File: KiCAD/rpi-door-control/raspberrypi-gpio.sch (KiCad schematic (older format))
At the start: 26 parts, among them IC1 4N35, J1 RJ45, P1 CONN_13X2, P2 CONN_2, P3 CONN_2, P4 CONN_2, Q1 2N3904, Q2 2N3904, SW1 SW_PUSH, U1 RELAY

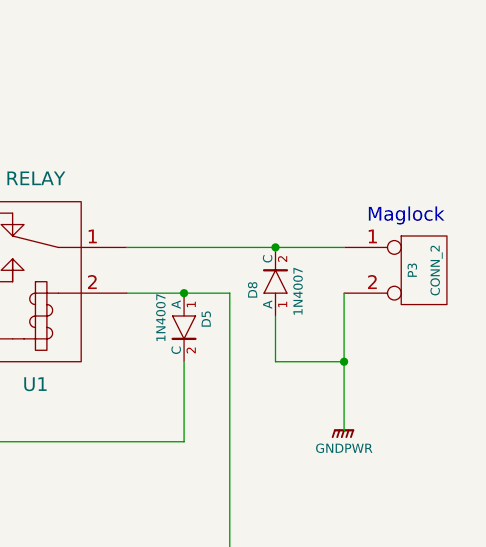
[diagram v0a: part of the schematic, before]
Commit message: Moved parts around on 12V side and aligned holes better
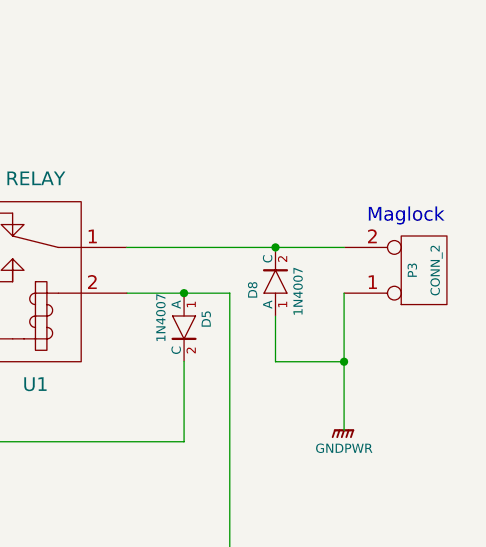
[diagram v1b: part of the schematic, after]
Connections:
- net GNDPWR: now also P3.1 (P1); no longer P3.2 (PM)
- net at D8.2 (C), U1.1: now also P3.2 (PM); no longer P3.1 (P1)
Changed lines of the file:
@@
 Sheet 1 2
 Title "Raspberry Pi Door Controller"
-Date "17 may 2014"
+Date "22 may 2014"
 Rev "0.6.1"
 Comp "Copyright 2014, Shawn Wilson"
@@
 F 4 "DE1632" V 10100 1900 60  0001 C CNN "dipmicro#"
 	1    10100 1900
-	1    0    0    -1
+	1    0    0    1
 $EndComp
 Text Notes 950  1050 0    60   ~ 0
